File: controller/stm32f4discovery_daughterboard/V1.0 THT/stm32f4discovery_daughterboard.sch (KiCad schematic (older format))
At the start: 69 parts, among them P1 CONN_25X2, P2 CONN_25X2, T1 BC547

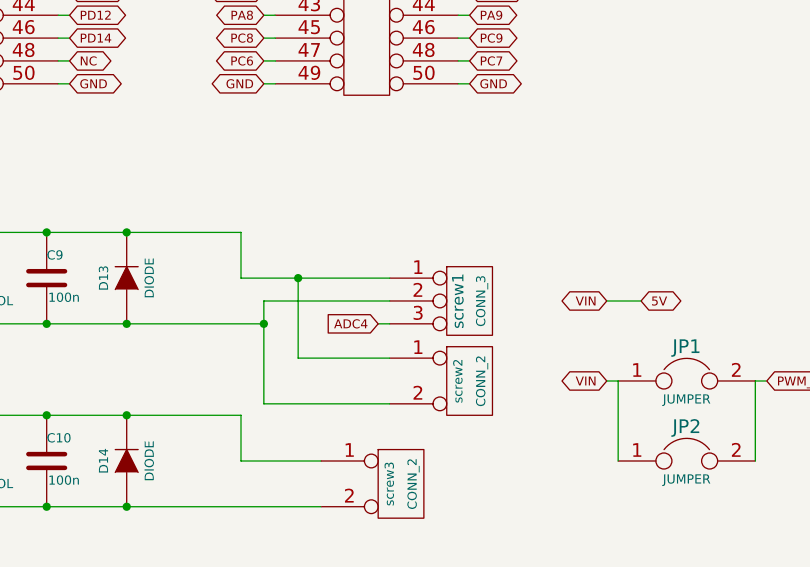
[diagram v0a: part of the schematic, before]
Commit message: fixed align of the main header
The Main pin header (for the dosvocery board) was offset in the previous
version.
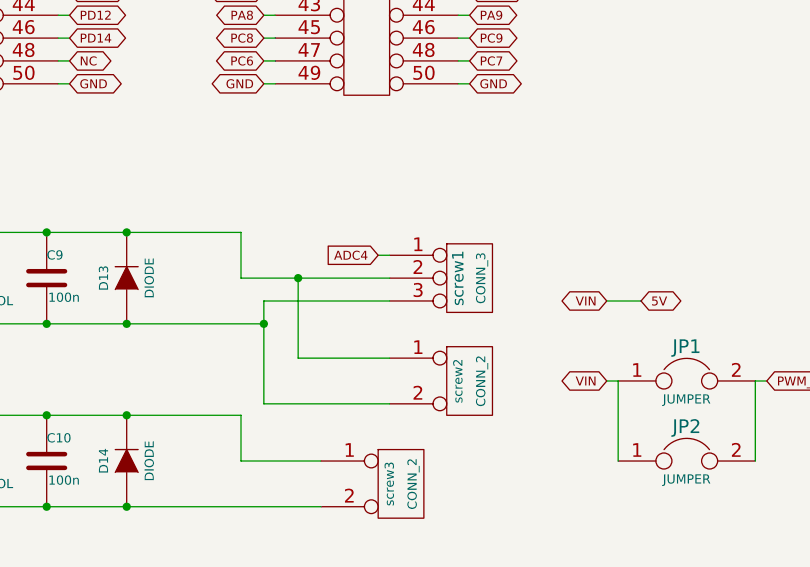
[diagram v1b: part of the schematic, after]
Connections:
- net 5V: now also screw1.2 (PM); no longer screw1.1 (P1)
- net ADC4: now also screw1.1 (P1); no longer screw1.3 (P3)
- net GND: now also screw1.3 (P3); no longer screw1.2 (PM)
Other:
- moved on the sheet: screw1
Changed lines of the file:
@@
 Sheet 1 1
 Title "STM32F4 Discovery Daughterboard Paparazzi"
-Date "11 apr 2014"
+Date "2 may 2014"
 Rev "V1.0"
 Comp ""
@@
 L CONN_3 screw1
 U 1 1 5333D051
-P 3800 4500
-F 0 "screw1" V 3750 4500 50  0000 C CNN
-F 1 "CONN_3" V 3850 4500 40  0000 C CNN
-F 2 "bornier3" H 3800 4500 60  0001 C CNN
-F 3 "~" H 3800 4500 60  0000 C CNN
-	1    3800 4500
-	1    0    0    -1
-$EndComp
-Text GLabel 3400 4600 0    39   Input ~ 0
+P 3800 4400
+F 0 "screw1" V 3750 4400 50  0000 C CNN
+F 1 "CONN_3" V 3850 4400 40  0000 C CNN
+F 2 "bornier3" H 3800 4400 60  0001 C CNN
+F 3 "~" H 3800 4400 60  0000 C CNN
+	1    3800 4400
+	1    0    0    -1
+$EndComp
+Text GLabel 3400 4300 0    39   Input ~ 0
 ADC4
 $Comp
@@
 	3450 4500 2900 4500
 Wire Wire Line
-	3400 4600 3450 4600
+	3400 4300 3450 4300
 Wire Wire Line
 	2350 7100 2350 7000

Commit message: added .pro and dxf outline
Updated with 2015-07-30 6023 on Windows. Added DXF file containing board
outline + holes.  Added KiCAD project file.
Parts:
- C1, C10, C2, C3, C4, C5, C6, C9: symbol C -> C-RESCUE-stm32f4discovery_daughterboard
- R1, R10, R11, R12, R13, R14, R15, R2, R3, R4, R5, R6, R7, R8, R9: symbol R -> R-RESCUE-stm32f4discovery_daughterboard
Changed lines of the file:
@@
 EESchema Schematic File Version 2
+LIBS:stm32f4discovery_daughterboard-rescue
 LIBS:power
 LIBS:device
@@
 LIBS:memory
 LIBS:xilinx
-LIBS:special
 LIBS:microcontrollers
 LIBS:dsp
@@
 LIBS:valves
 LIBS:stm32f4discovery_daughterboard-cache
-EELAYER 27 0
+EELAYER 25 0
 EELAYER END
 $Descr A4 11693 8268
@@
 BOOT0
 $Comp
-L R R1
+L R-RESCUE-stm32f4discovery_daughterboard R1
 U 1 1 53306EC7
 P 1000 6350
@@
 $EndComp
 $Comp
-L R R2
+L R-RESCUE-stm32f4discovery_daughterboard R2
 U 1 1 53306ED4
 P 1000 6850
@@
 3V
 $Comp
-L R R3
+L R-RESCUE-stm32f4discovery_daughterboard R3
 U 1 1 53306F32
 P 2050 6350
@@
 $EndComp
 $Comp
-L R R4
+L R-RESCUE-stm32f4discovery_daughterboard R4
 U 1 1 53306F38
 P 2050 6850
@@
 3V
 $Comp
-L R R5
+L R-RESCUE-stm32f4discovery_daughterboard R5
 U 1 1 53306F54
 P 3100 6350
@@
 $EndComp
 $Comp
-L R R6
+L R-RESCUE-stm32f4discovery_daughterboard R6
 U 1 1 53306F5A
 P 3100 6850
@@
 3V
 $Comp
-L R R7
+L R-RESCUE-stm32f4discovery_daughterboard R7
 U 1 1 53306F76
 P 4150 6350
@@
 $EndComp
 $Comp
-L R R8
+L R-RESCUE-stm32f4discovery_daughterboard R8
 U 1 1 53306F7C
 P 4150 6850
@@
 3V
 $Comp
-L R R9
+L R-RESCUE-stm32f4discovery_daughterboard R9
 U 1 1 53306F98
 P 5200 6350
@@
 $EndComp
 $Comp
-L R R10
+L R-RESCUE-stm32f4discovery_daughterboard R10
 U 1 1 53306F9E
 P 5200 6850
@@
 3V
 $Comp
-L R R11
+L R-RESCUE-stm32f4discovery_daughterboard R11
 U 1 1 53306FBA
 P 6250 6350
@@
 $EndComp
 $Comp
-L R R12
+L R-RESCUE-stm32f4discovery_daughterboard R12
 U 1 1 53306FC0
 P 6250 6850
@@
 $EndComp
 $Comp
-L R R13
+L R-RESCUE-stm32f4discovery_daughterboard R13
 U 1 1 5331F861
 P 9700 5350
@@
 VIN
 $Comp
-L C C2
+L C-RESCUE-stm32f4discovery_daughterboard C2
 U 1 1 5331FFE7
 P 2600 6800
@@
 GND
 $Comp
-L R R14
+L R-RESCUE-stm32f4discovery_daughterboard R14
 U 1 1 5332FC66
 P 4700 2900
@@
 $EndComp
 $Comp
-L R R15
+L R-RESCUE-stm32f4discovery_daughterboard R15
 U 1 1 53330136
 P 5350 2300
@@
 ADC4
 $Comp
-L C C1
+L C-RESCUE-stm32f4discovery_daughterboard C1
 U 1 1 5334159B
 P 1550 6800
@@
 $EndComp
 $Comp
-L C C3
+L C-RESCUE-stm32f4discovery_daughterboard C3
 U 1 1 533415A1
 P 3650 6800
@@
 $EndComp
 $Comp
-L C C4
+L C-RESCUE-stm32f4discovery_daughterboard C4
 U 1 1 533415A7
 P 4700 6800
@@
 $EndComp
 $Comp
-L C C5
+L C-RESCUE-stm32f4discovery_daughterboard C5
 U 1 1 533415AD
 P 5750 6800
@@
 $EndComp
 $Comp
-L C C6
+L C-RESCUE-stm32f4discovery_daughterboard C6
 U 1 1 533415B3
 P 6800 6800
@@
 $EndComp
 $Comp
-L C C9
+L C-RESCUE-stm32f4discovery_daughterboard C9
 U 1 1 53430CB7
 P 1950 4400
@@
 $EndComp
 $Comp
-L C C10
+L C-RESCUE-stm32f4discovery_daughterboard C10
 U 1 1 53430CBD
 P 1950 5200
